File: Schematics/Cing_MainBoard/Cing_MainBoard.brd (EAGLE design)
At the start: 100 x 100 mm, 85 parts, among them IC1 L293D, IC3 FT232RL, Q1 16mhz, U2 BMP180, U3 MPU-6050MPU6050

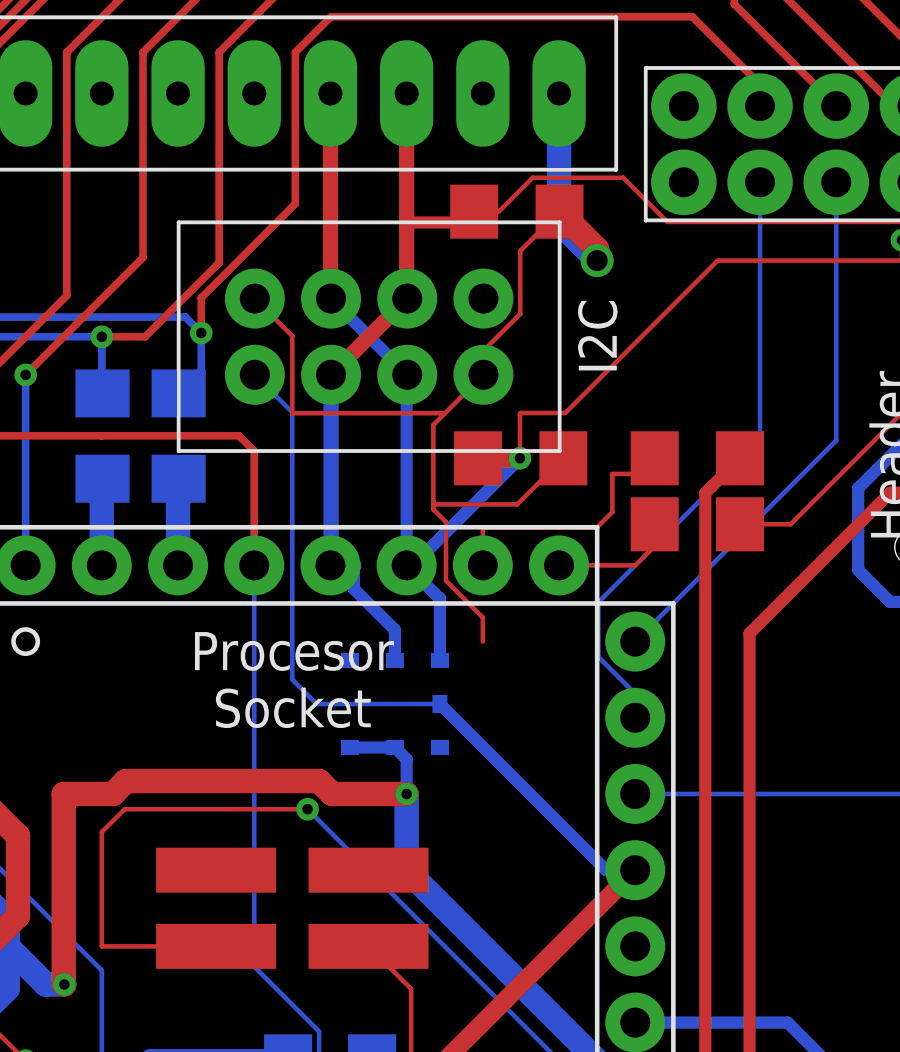
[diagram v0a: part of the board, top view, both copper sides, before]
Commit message: Adding pin 36
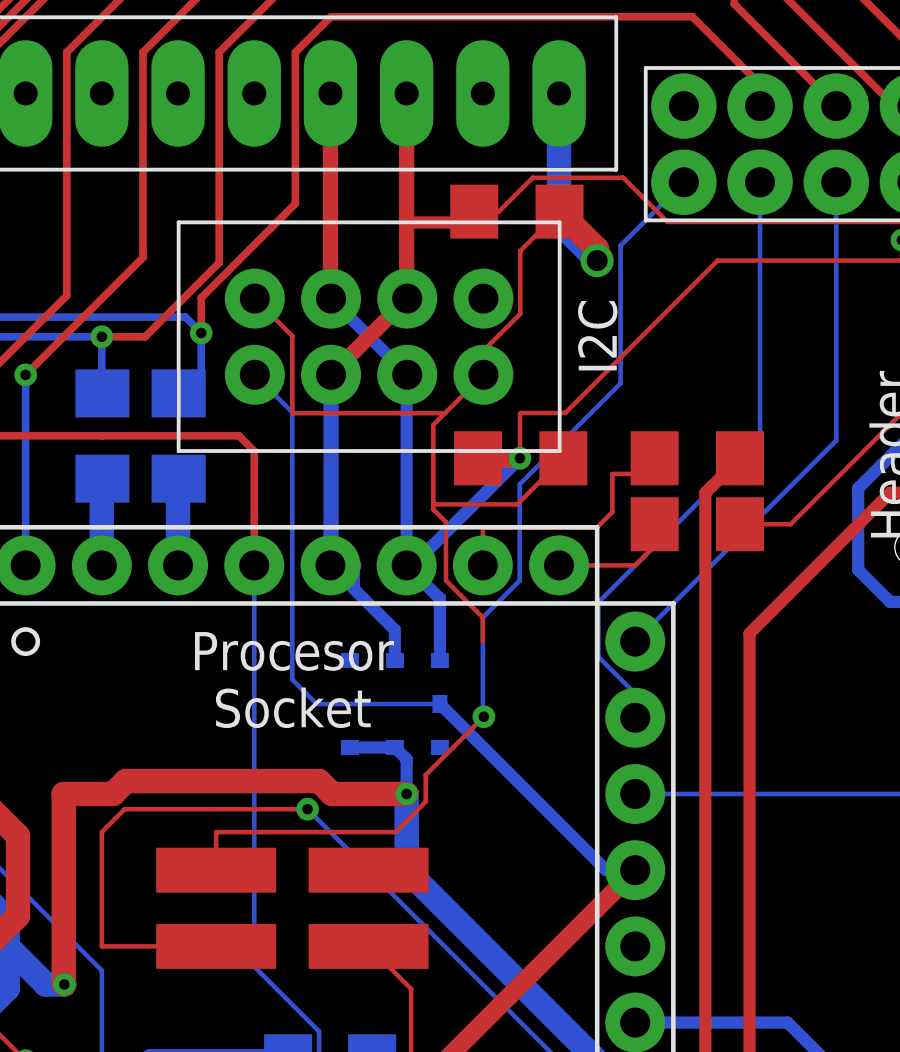
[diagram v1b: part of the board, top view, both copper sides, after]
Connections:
- new net 36: U$1.36, U$2.+5V1
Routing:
- net 36: track 0.00 -> 33.0 mm, vias 0 -> 1
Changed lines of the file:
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@@
 <wire x1="-46.0326" y1="-19.0174" x2="-46" y2="-19.05" width="0.1524" layer="1"/>
+</signal>
+<signal name="36">
+<contactref element="U$1" pad="36"/>
+<contactref element="U$2" pad="+5V1"/>
+<wire x1="13.05" y1="24.2" x2="10.9418" y2="22.0918" width="0.1524" layer="16"/>
+<wire x1="6.35" y1="9.69249375" x2="6.35" y2="6.35" width="0.1524" layer="16"/>
+<wire x1="7.5786" y1="10.92109375" x2="6.35" y2="9.69249375" width="0.1524" layer="16"/>
+<wire x1="7.5786" y1="14.13345" x2="7.5786" y2="10.92109375" width="0.1524" layer="16"/>
+<wire x1="10.9418" y1="22.0918" x2="10.9418" y2="17.49665" width="0.1524" layer="16"/>
+<wire x1="10.9418" y1="17.49665" x2="7.5786" y2="14.13345" width="0.1524" layer="16"/>
+<wire x1="6.35" y1="6.35" x2="6.383875" y2="6.383875" width="0.1524" layer="16"/>
+<via x="6.383875" y="6.383875" extent="1-16" drill="0.35"/>
+<wire x1="6.383875" y1="6.383875" x2="4.445" y2="4.445" width="0.1524" layer="1"/>
+<wire x1="4.445" y1="4.445" x2="4.445" y2="3.54696875" width="0.1524" layer="1"/>
+<wire x1="4.445" y1="3.54696875" x2="3.43803125" y2="2.54" width="0.1524" layer="1"/>
+<wire x1="3.43803125" y1="2.54" x2="-2.54" y2="2.54" width="0.1524" layer="1"/>
+<wire x1="-2.54" y1="2.54" x2="-2.54" y2="1.27" width="0.1524" layer="1"/>
 </signal>
 </signals>

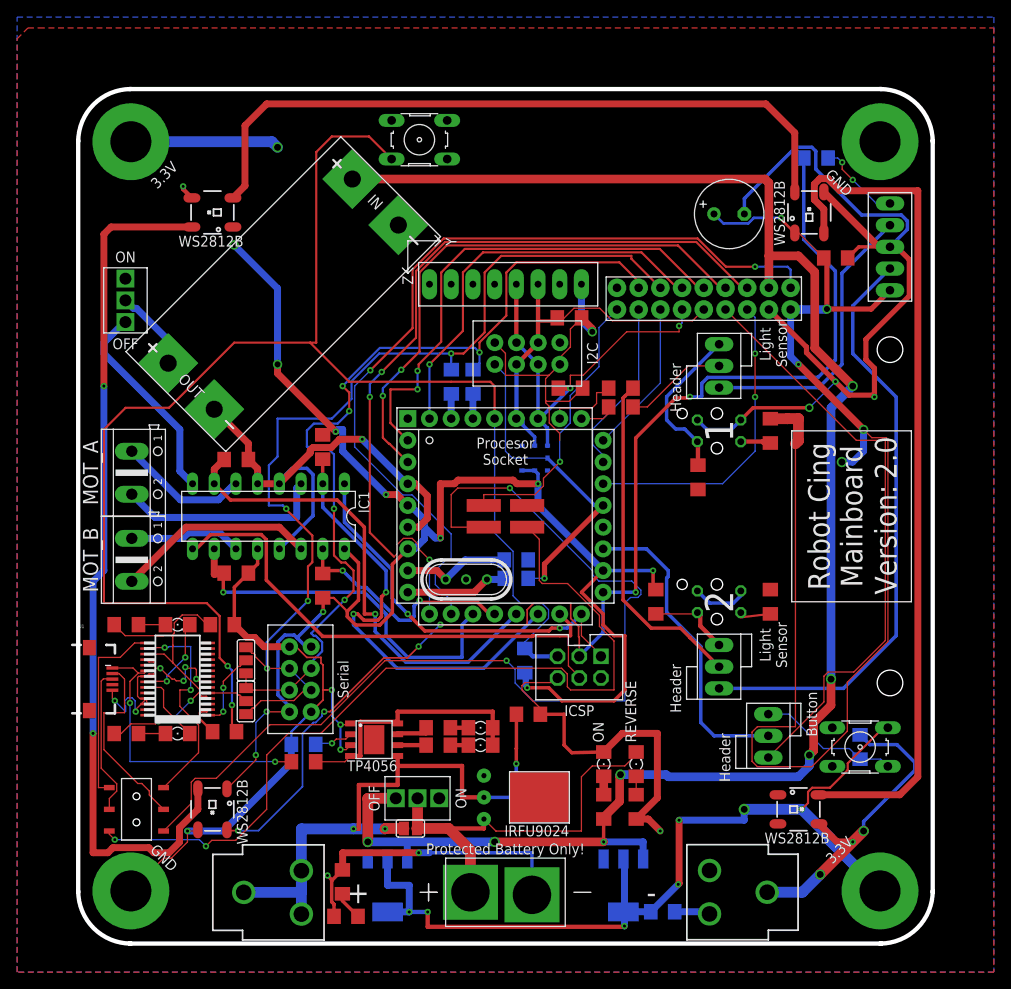
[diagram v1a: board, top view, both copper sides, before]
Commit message: Adding optional 3V3 regulator
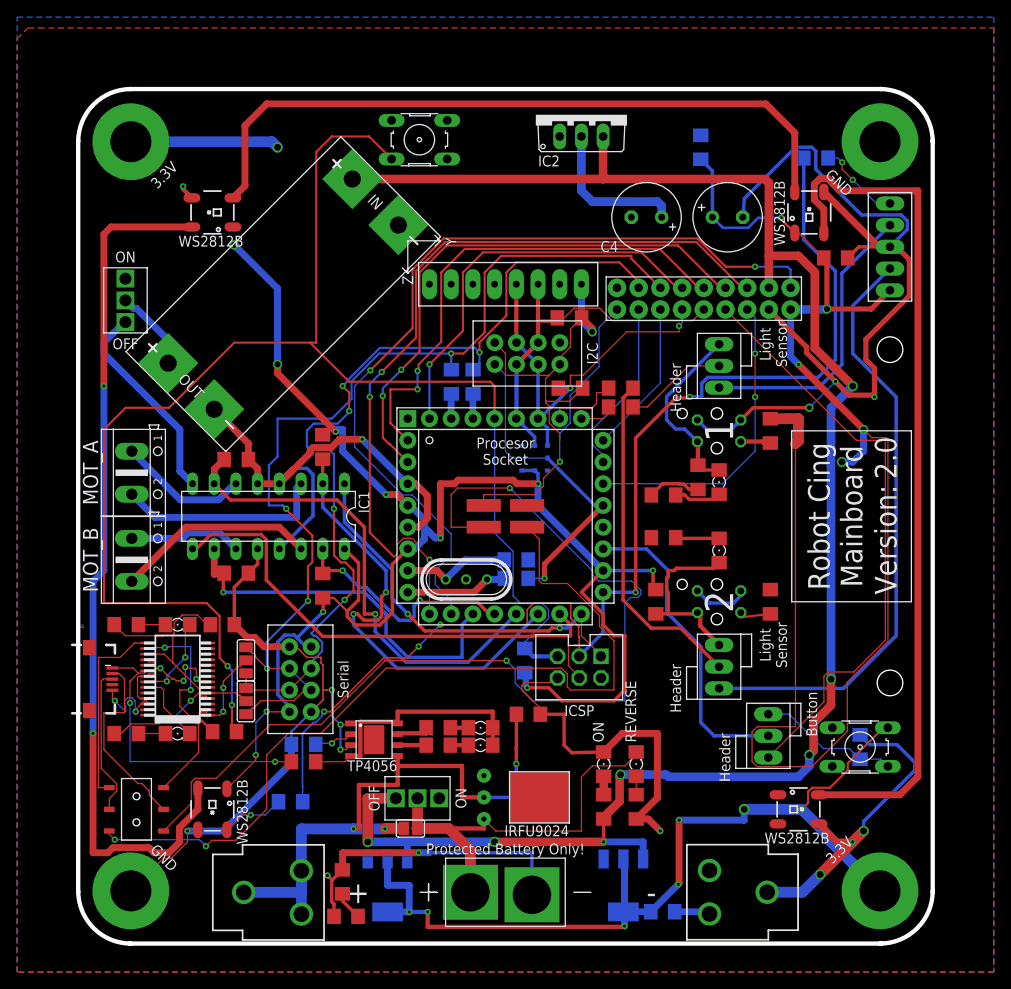
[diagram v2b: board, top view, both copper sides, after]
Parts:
- added C4: 100uf, rcl:E3,5-8
- added C5: 100n, rcl:C1206
- added IC2: LM1117T3.3-V, Cing Library:LM1117T
- added R10, R20, R7: 1k, rcl:R1206
- added TXD1: LightSensor 1, led:1206
- added TXD2: LightSensor 2, led:1206
- moved C6 0.42 mm to (26.0, 35.0)
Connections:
- new net N$12: LED5.4, R7.1
- new net N$15: R10.1, TXD1.A
- new net N$17: R20.1, TXD2.A
- net +3V3: now also C4.+, C5.1, IC2.2, R10.2, R20.2
- net BAT+: now also IC2.3
- net GND: now also C4.-, C5.2, IC2.1
- net N$24: now also TXD1.C
- net N$45: now also TXD2.C
- net SCK: now also R7.2; no longer LED5.4
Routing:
- net +3V3: track 523.2 -> 555.1 mm
- net N$45: track 9.76 -> 26.2 mm
- net SCK: track 146.5 -> 137.3 mm, vias 6 -> 5
- net N$12: track 0.00 -> 7.38 mm, vias 0 -> 1
- net N$15: track 0.00 -> 5.54 mm
- net N$17: track 0.00 -> 5.11 mm
- net BAT+: track 205.1 -> 210.1 mm
- net N$24: track 18.8 -> 21.5 mm
